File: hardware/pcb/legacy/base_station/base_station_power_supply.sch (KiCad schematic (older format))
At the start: 19 parts, among them SW1 SWITCH

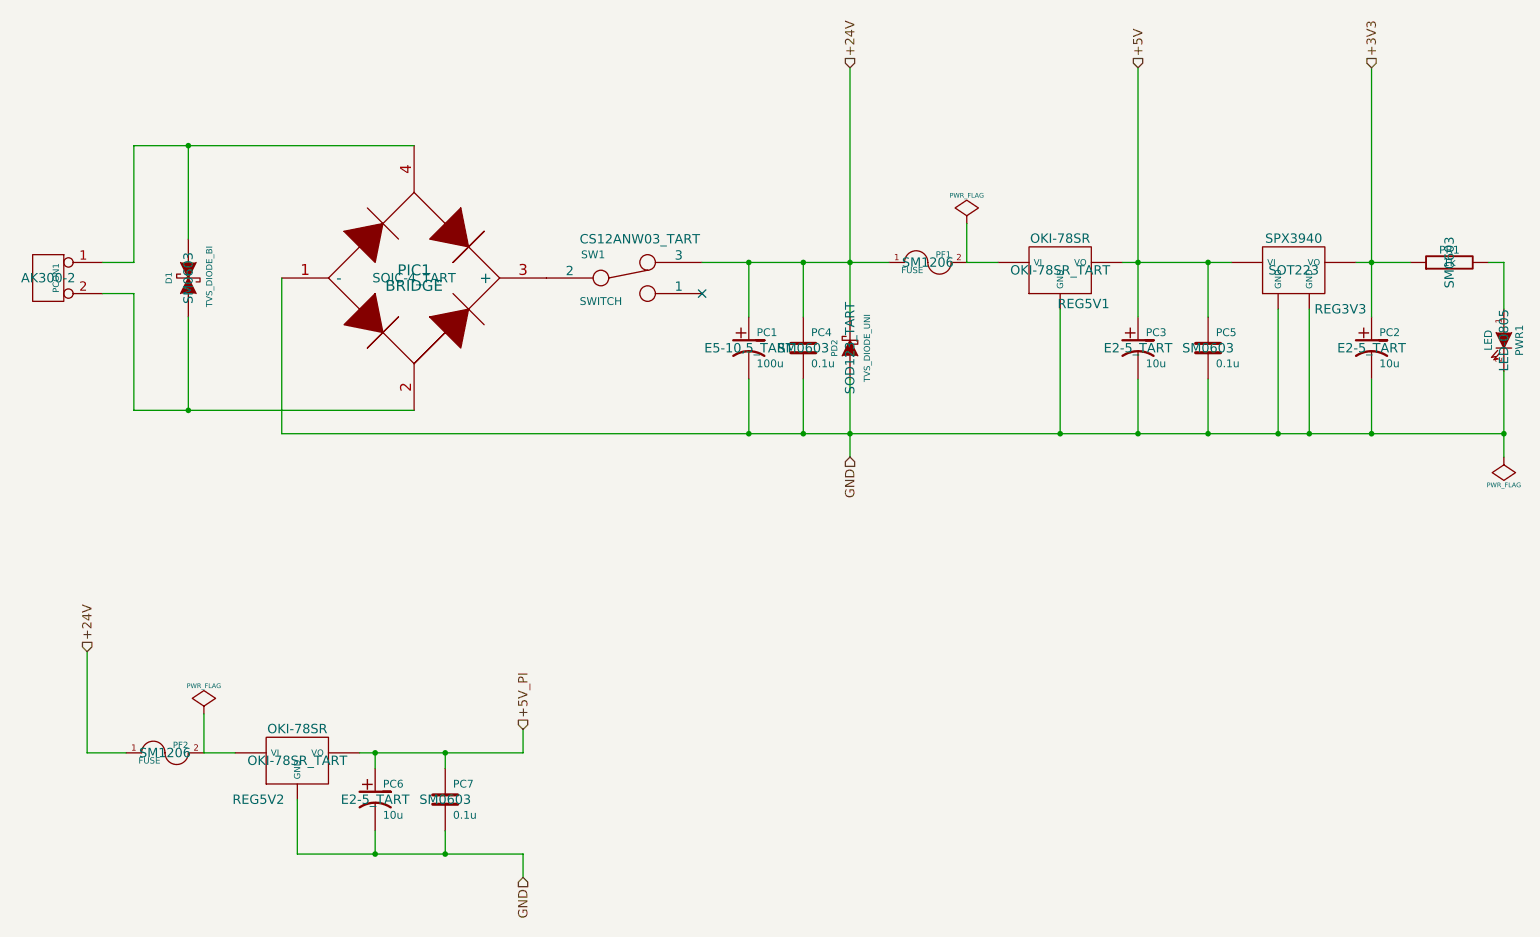
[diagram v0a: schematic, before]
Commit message: Moved things around so that old files are in the legacy directory
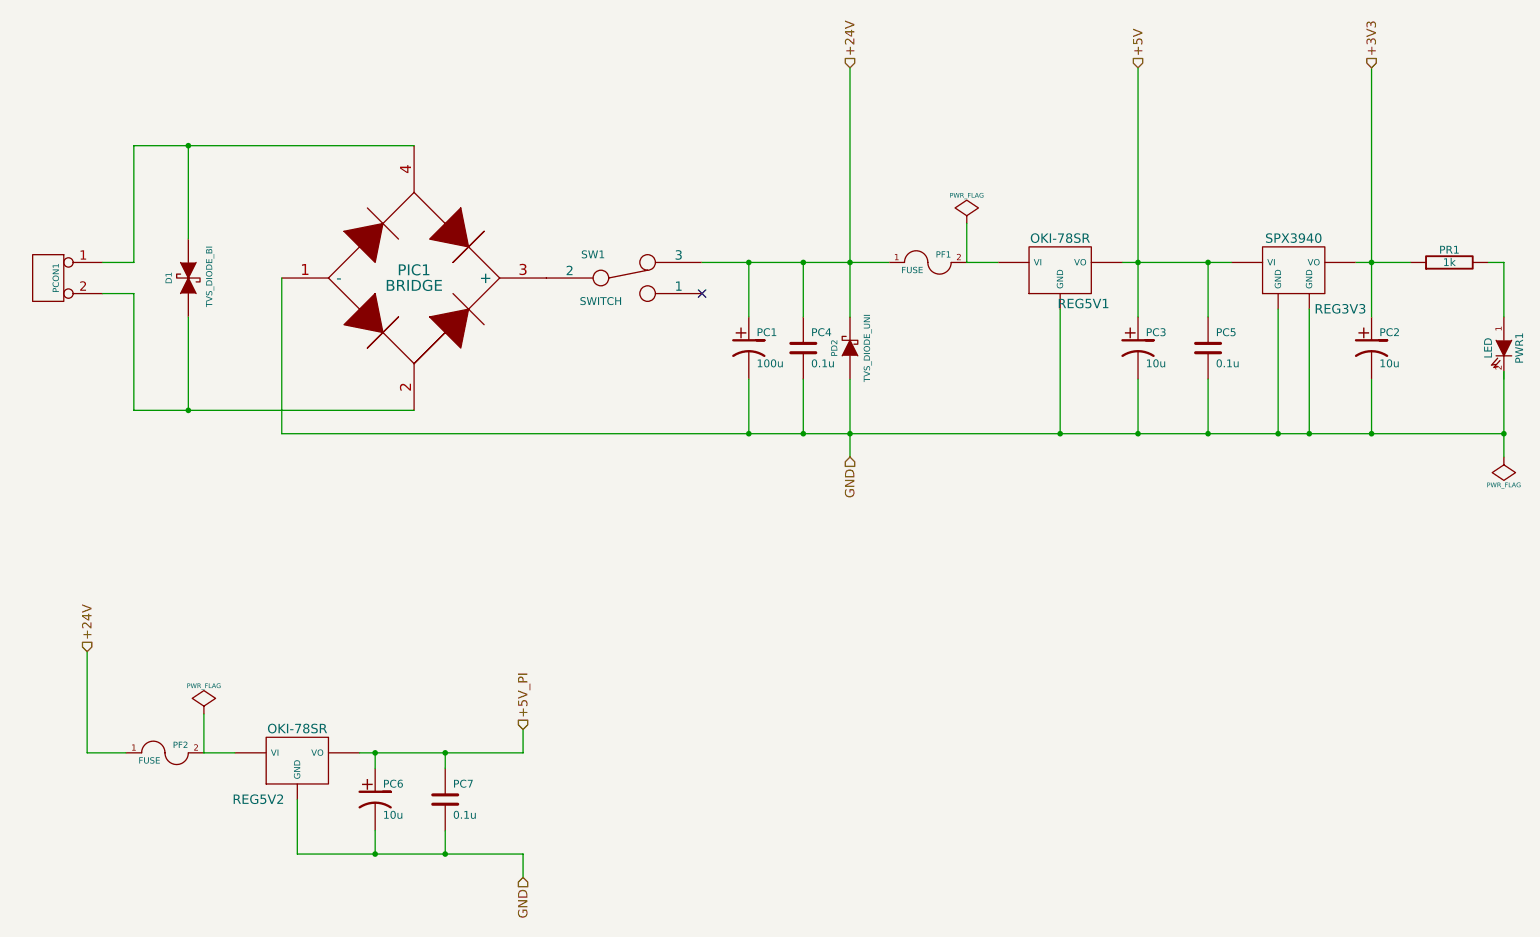
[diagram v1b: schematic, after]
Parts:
- D1, PC4, PC5, PC7, PR1: footprint SM0603 -> (none)
- PC3, PC6: footprint E2-5_TART -> E5-10,5_TART
- PCON1: footprint AK300-2 -> (none)
- PD2: footprint SOD123_TART -> (none)
- PF1, PF2: footprint SM1206 -> (none)
- PIC1: footprint SOIC-4_TART -> (none)
- PWR1: footprint LED-0805 -> (none)
- REG3V3: footprint SOT223 -> (none)
- REG5V1, REG5V2: footprint OKI-78SR_TART -> (none)
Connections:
- net GND: no longer PWR1.2 (K)
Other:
- moved on the sheet: PWR1
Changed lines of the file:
@@
 Sheet 2 7
 Title ""
-Date "13 feb 2015"
+Date "8 dec 2014"
 Rev ""
 Comp ""
@@
 F 0 "PF2" H 1950 5550 40  0000 C CNN
 F 1 "FUSE" H 1750 5450 40  0000 C CNN
-F 2 "SM1206" H 1850 5500 60  0000 C CNN
+F 2 "" H 1850 5500 60  0001 C CNN
 F 3 "" H 1850 5500 60  0001 C CNN
 	1    1850 5500
@@
 F 0 "PC6" H 3250 5900 50  0000 L CNN
 F 1 "10u" H 3250 5700 50  0000 L CNN
-F 2 "E2-5_TART" H 3200 5800 60  0000 C CNN
+F 2 "E5-10,5_TART" H 3200 5800 60  0001 C CNN
 F 3 "" H 3200 5800 60  0001 C CNN
 	1    3200 5800
@@
 F 0 "PC7" H 3700 5900 50  0000 L CNN
 F 1 "0.1u" H 3700 5700 50  0000 L CNN
-F 2 "SM0603" H 3650 5800 60  0000 C CNN
+F 2 "" H 3650 5800 60  0001 C CNN
 F 3 "" H 3650 5800 60  0001 C CNN
 	1    3650 5800
@@
 F 0 "REG5V2" H 2450 5300 60  0000 C CNN
 F 1 "OK1-78SR_TART" H 2700 5860 60  0001 C CNN
-F 2 "OKI-78SR_TART" H 2700 5550 60  0000 C CNN
+F 2 "" H 2700 5550 60  0001 C CNN
 F 3 "" H 2700 5550 60  0001 C CNN
 F 4 "OKI-78SR" H 2700 5754 60  0000 C CNN "NAME"
@@
 F 0 "REG3V3" H 9400 2150 60  0000 C CNN
 F 1 "SPX3940_TART" H 9100 2710 60  0001 C CNN
-F 2 "SOT223" H 9100 2400 60  0000 C CNN
+F 2 "" H 9100 2400 60  0001 C CNN
 F 3 "" H 9100 2400 60  0001 C CNN
 F 4 "SPX3940" H 9100 2604 60  0000 C CNN "NAME"
@@
 F 0 "REG5V1" H 7750 2184 60  0000 C CNN
 F 1 "OK1-78SR_TART" H 7600 2710 60  0001 C CNN
-F 2 "OKI-78SR_TART" H 7600 2400 60  0000 C CNN
+F 2 "" H 7600 2400 60  0001 C CNN
 F 3 "" H 7600 2400 60  0001 C CNN
 F 4 "OKI-78SR" H 7600 2604 60  0000 C CNN "NAME"
@@
 F 0 "D1" H 2000 2575 40  0000 C CNN
 F 1 "TVS_DIODE_BI_TART" H 1980 2645 40  0001 C CNN
-F 2 "SM0603" H 2000 2450 60  0000 C CNN
+F 2 "" H 2000 2450 60  0001 C CNN
 F 3 "" H 2000 2450 60  0001 C CNN
 F 4 "TVS_DIODE_BI" H 2010 2315 40  0000 C CNN "NAME"
@@
 F 0 "PD2" H 6250 3000 40  0000 C CNN
 F 1 "TVS_DIODE_UNI_TART" H 6240 3060 40  0001 C CNN
-F 2 "SOD123_TART" H 6250 2900 60  0000 C CNN
+F 2 "" H 6250 2900 60  0001 C CNN
 F 3 "" H 6250 2900 60  0001 C CNN
 F 4 "TVS_DIODE_UNI" H 6250 2790 40  0000 C CNN "NAME"
@@
 F 0 "PIC1" H 3450 2500 70  0000 C CNN
 F 1 "BRIDGE_TART" H 4000 3400 60  0001 C CNN
-F 2 "SOIC-4_TART" H 3450 2450 60  0000 C CNN
+F 2 "" H 3450 2450 60  0001 C CNN
 F 3 "" H 3450 2450 60  0001 C CNN
 F 4 "MICRO COMMERCIAL" H 4150 3300 60  0001 C CNN "MANUFAC"
@@
 F 0 "PC4" H 6000 3000 50  0000 L CNN
 F 1 "0.1u" H 6000 2800 50  0000 L CNN
-F 2 "SM0603" H 5950 2900 60  0000 C CNN
+F 2 "" H 5950 2900 60  0001 C CNN
 F 3 "" H 5950 2900 60  0001 C CNN
 	1    5950 2900
@@
 F 0 "PC1" H 5650 3000 50  0000 L CNN
 F 1 "100u" H 5650 2800 50  0000 L CNN
-F 2 "E5-10,5_TART" H 5600 2900 60  0000 C CNN
+F 2 "E5-10,5_TART" H 5600 2900 60  0001 C CNN
 F 3 "" H 5600 2900 60  0001 C CNN
 	1    5600 2900
@@
 F 0 "PF1" H 6850 2400 40  0000 C CNN
 F 1 "FUSE" H 6650 2300 40  0000 C CNN
-F 2 "SM1206" H 6750 2350 60  0000 C CNN
+F 2 "" H 6750 2350 60  0001 C CNN
 F 3 "" H 6750 2350 60  0001 C CNN
 	1    6750 2350
@@
 L LED PWR1
 U 1 1 5407A3D9
-P 10450 2850
-F 0 "PWR1" H 10450 2950 50  0000 C CNN
-F 1 "LED" H 10450 2750 50  0000 C CNN
-F 2 "LED-0805" H 10450 2850 60  0000 C CNN
-F 3 "" H 10450 2850 60  0001 C CNN
-	1    10450 2850
+P 10450 2900
+F 0 "PWR1" H 10450 3000 50  0000 C CNN
+F 1 "LED" H 10450 2800 50  0000 C CNN
+F 2 "" H 10450 2900 60  0001 C CNN
+F 3 "" H 10450 2900 60  0001 C CNN
+	1    10450 2900
 	0    1    1    0
 $EndComp
@@
 F 0 "PR1" V 10180 2350 50  0000 C CNN
 F 1 "1k" V 10100 2350 50  0000 C CNN
-F 2 "SM0603" H 10100 2350 60  0000 C CNN
+F 2 "" H 10100 2350 60  0001 C CNN
 F 3 "" H 10100 2350 60  0001 C CNN
 	1    10100 2350
@@
 F 0 "PC2" H 9650 3000 50  0000 L CNN
 F 1 "10u" H 9650 2800 50  0000 L CNN
-F 2 "E2-5_TART" H 9600 2900 60  0000 C CNN
+F 2 "E2-5_TART" H 9600 2900 60  0001 C CNN
 F 3 "" H 9600 2900 60  0001 C CNN
 	1    9600 2900
@@
 F 0 "PC5" H 8600 3000 50  0000 L CNN
 F 1 "0.1u" H 8600 2800 50  0000 L CNN
-F 2 "SM0603" H 8550 2900 60  0000 C CNN
+F 2 "" H 8550 2900 60  0001 C CNN
 F 3 "" H 8550 2900 60  0001 C CNN
 	1    8550 2900
@@
 F 0 "PC3" H 8150 3000 50  0000 L CNN
 F 1 "10u" H 8150 2800 50  0000 L CNN
-F 2 "E2-5_TART" H 8100 2900 60  0000 C CNN
+F 2 "E5-10,5_TART" H 8100 2900 60  0001 C CNN
 F 3 "" H 8100 2900 60  0001 C CNN
 	1    8100 2900
@@
 F 0 "PCON1" V 1050 2450 40  0000 C CNN
 F 1 "~" V 1150 2450 40  0000 C CNN
-F 2 "AK300-2" H 1100 2450 60  0000 C CNN
+F 2 "" H 1100 2450 60  0000 C CNN
 F 3 "" H 1100 2450 60  0000 C CNN
 	1    1100 2450
@@
 F 0 "SW1" H 4600 2600 50  0000 C CNN
 F 1 "SWITCH" H 4650 2300 50  0000 C CNN
-F 2 "CS12ANW03_TART" H 4900 2700 60  0000 C CNN
+F 2 "CS12ANW03_TART" H 4900 2700 60  0001 C CNN
 F 3 "~" H 4800 2450 60  0000 C CNN
 	1    4800 2450
@@
 	10450 2350 10350 2350
 Wire Wire Line
-	10450 2650 10450 2350
+	10450 2700 10450 2350
 Wire Wire Line
 	7000 2350 7200 2350
